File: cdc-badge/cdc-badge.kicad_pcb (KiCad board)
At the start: 4 copper layers, 85 x 110 mm, 158 parts, among them J1 USB_C, J2 JST S2B-PH-SM4-TB, J3 Conn_02x20_Odd_Even, J4 Conn_Grove, J5 Conn_02x03_Odd_Even, J6 Conn_01x06, J7 Conn_01x24, Q1 Si1308EDL, Q2 Si1308EDL, SW0 0, SW1 1, SW10 YES, SW11 NO, SW12 power on/reset, SW13 reset, SW14 flash/power off, SW15 MST-22D18G2 3J, SW16 MST-22D18G2 3J, SW2 2, SW3 3, SW4 4, SW5 5, SW6 6, SW7 7, SW8 8, SW9 9, U1 ESP32-S3-WROOM-1-N16R8, U2 TCA9535PWR, U3 TR01-C2P-T301, U5 TLV61070ADBVR, U6 BQ25895RTW, U8 TLV62569DBV

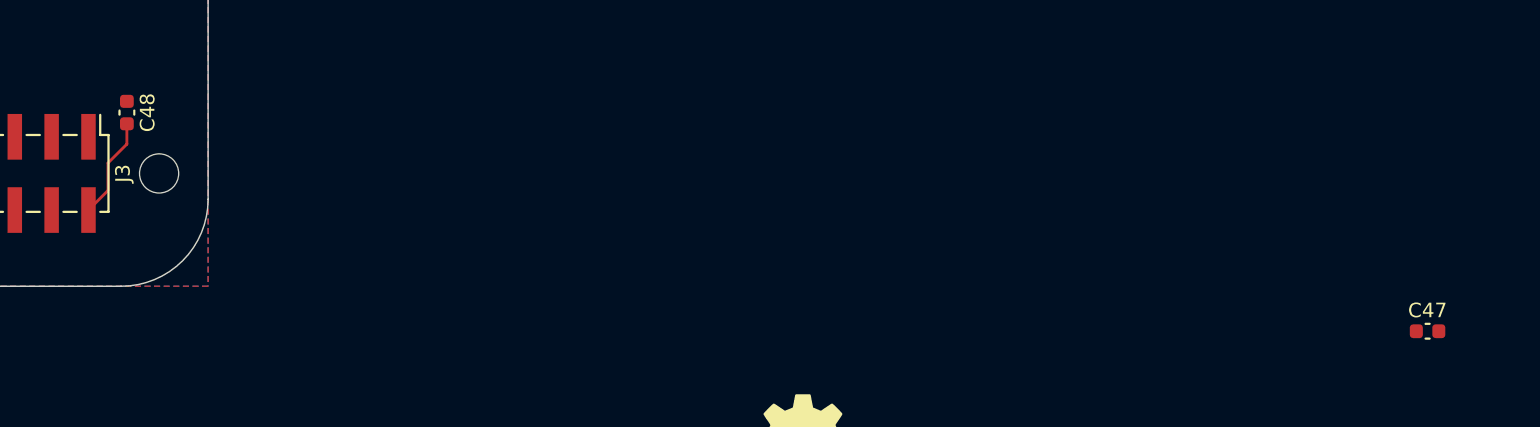
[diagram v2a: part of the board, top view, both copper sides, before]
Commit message: PCB: place caps to 3.3v and 5v pins at raspi conn.
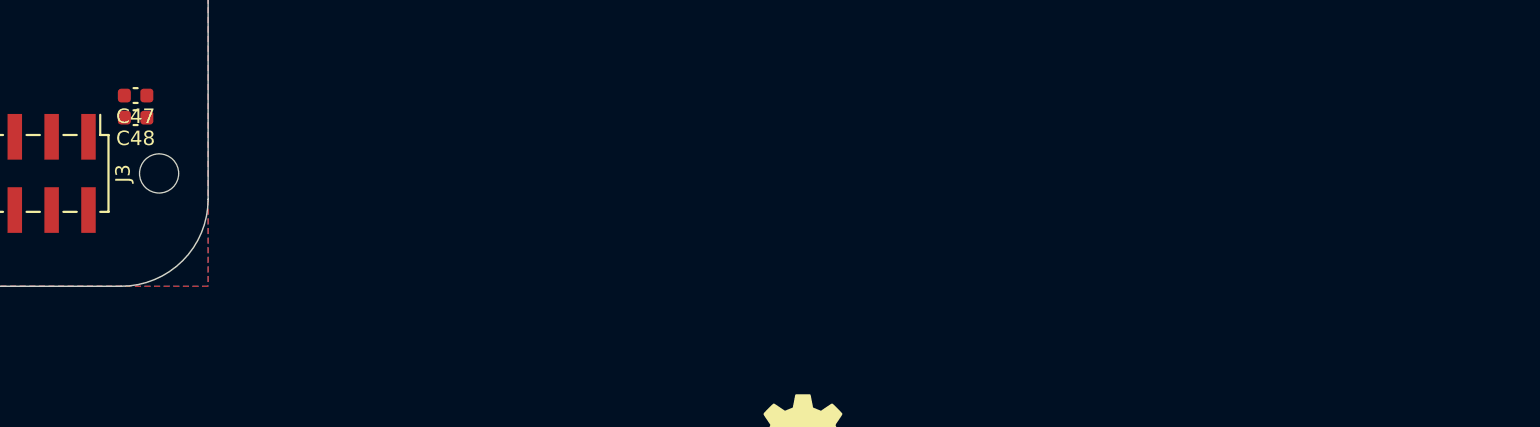
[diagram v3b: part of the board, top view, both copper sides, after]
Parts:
- moved C47 90.5 mm to (135.0, 145.8), turned to 180 degrees
- moved C48 0.69 mm to (135.0, 147.4), turned to 180 degrees
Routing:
- net +5V: track 8.72 -> 1.68 mm
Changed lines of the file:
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@@
 	(footprint "Capacitor_SMD:C_0603_1608Metric"
 		(layer "F.Cu")
-		(at 224.075 162.1)
+		(at 135 145.85 180)
 		(descr "Capacitor SMD 0603 (1608 Metric), square (rectangular) end terminal, IPC-7351 nominal, (Body size source: IPC-SM-782 page 76, https://www.pcb-3d.com/wordpress/wp-content/uploads/ipc-sm-782a_amendment_1_and_2.pdf), generated with kicad-footprint-generator")
 		(tags "capacitor")
@@
 		)
 		(property "MPN" "CL10A105KB8NNNC"
-			(at 0 0 0)
+			(at 0 0 180)
 			(unlocked yes)
 			(layer "F.Fab")
@@
 		)
 		(property "JLCPCB PN" "C15849"
-			(at 0 0 0)
+			(at 0 0 180)
 			(unlocked yes)
 			(layer "F.Fab")
@@
 		(attr smd)
 		(fp_line
-			(start -0.14058 -0.51)
-			(end 0.14058 -0.51)
+			(start -0.14058 0.51)
+			(end 0.14058 0.51)
 			(stroke
 				(width 0.153)
@@
 		)
 		(fp_line
-			(start -0.14058 0.51)
-			(end 0.14058 0.51)
+			(start -0.14058 -0.51)
+			(end 0.14058 -0.51)
 			(stroke
 				(width 0.153)
@@
 		)
 		(fp_line
-			(start -1.48 -0.73)
-			(end 1.48 -0.73)
+			(start 1.48 0.73)
+			(end -1.48 0.73)
 			(stroke
 				(width 0.05)
@@
 		)
 		(fp_line
-			(start -1.48 0.73)
-			(end -1.48 -0.73)
+			(start 1.48 -0.73)
+			(end 1.48 0.73)
 			(stroke
 				(width 0.05)
@@
 		)
 		(fp_line
-			(start 1.48 -0.73)
-			(end 1.48 0.73)
+			(start -1.48 0.73)
+			(end -1.48 -0.73)
 			(stroke
 				(width 0.05)
@@
 		)
 		(fp_line
-			(start 1.48 0.73)
-			(end -1.48 0.73)
+			(start -1.48 -0.73)
+			(end 1.48 -0.73)
 			(stroke
 				(width 0.05)
@@
 		)
 		(fp_line
-			(start -0.8 -0.4)
-			(end 0.8 -0.4)
+			(start 0.8 0.4)
+			(end -0.8 0.4)
 			(stroke
 				(width 0.1)
@@
 		)
 		(fp_line
-			(start -0.8 0.4)
-			(end -0.8 -0.4)
+			(start 0.8 -0.4)
+			(end 0.8 0.4)
 			(stroke
 				(width 0.1)
@@
 		)
 		(fp_line
-			(start 0.8 -0.4)
-			(end 0.8 0.4)
+			(start -0.8 0.4)
+			(end -0.8 -0.4)
 			(stroke
 				(width 0.1)
@@
 		)
 		(fp_line
-			(start 0.8 0.4)
-			(end -0.8 0.4)
+			(start -0.8 -0.4)
+			(end 0.8 -0.4)
 			(stroke
 				(width 0.1)
@@
 		)
 		(pad "1" smd roundrect
-			(at -0.775 0)
+			(at -0.775 0 180)
 			(size 0.9 0.95)
 			(layers "F.Cu" "F.Mask" "F.Paste")
@@
 		)
 		(pad "2" smd roundrect
-			(at 0.775 0)
+			(at 0.775 0 180)
 			(size 0.9 0.95)
 			(layers "F.Cu" "F.Mask" "F.Paste")
@@
 	(footprint "Capacitor_SMD:C_0603_1608Metric"
 		(layer "F.Cu")
-		(at 134.4 147.025 -90)
+		(at 135 147.375 180)
 		(descr "Capacitor SMD 0603 (1608 Metric), square (rectangular) end terminal, IPC-7351 nominal, (Body size source: IPC-SM-782 page 76, https://www.pcb-3d.com/wordpress/wp-content/uploads/ipc-sm-782a_amendment_1_and_2.pdf), generated with kicad-footprint-generator")
 		(tags "capacitor")
 		(property "Reference" "C48"
-			(at 0 -1.43 90)
+			(at 0 -1.43 0)
 			(layer "F.SilkS")
 			(effects
@@
 		)
 		(property "Value" "1uF"
-			(at 0 1.43 90)
+			(at 0 1.43 0)
 			(layer "F.Fab")
 			(effects
@@
 		)
 		(property "Datasheet" "~"
-			(at 0 0 90)
+			(at 0 0 0)
 			(layer "F.Fab")
 			(hide yes)
@@
 		)
 		(property "Description" "1uF 50V X5R ±10% 0603 Multilayer Ceramic Capacitor"
-			(at 0 0 90)
+			(at 0 0 0)
 			(layer "F.Fab")
 			(hide yes)
@@
 		)
 		(property "MPN" "CL10A105KB8NNNC"
-			(at 0 0 270)
+			(at 0 0 180)
 			(unlocked yes)
 			(layer "F.Fab")
@@
 		)
 		(property "JLCPCB PN" "C15849"
-			(at 0 0 270)
+			(at 0 0 180)
 			(unlocked yes)
 			(layer "F.Fab")
@@
 		)
 		(fp_line
-			(start -1.48 0.73)
-			(end -1.48 -0.73)
+			(start 1.48 0.73)
+			(end -1.48 0.73)
 			(stroke
 				(width 0.05)
@@
 		)
 		(fp_line
-			(start 1.48 0.73)
-			(end -1.48 0.73)
+			(start 1.48 -0.73)
+			(end 1.48 0.73)
 			(stroke
 				(width 0.05)
@@
 		)
 		(fp_line
-			(start -1.48 -0.73)
-			(end 1.48 -0.73)
+			(start -1.48 0.73)
+			(end -1.48 -0.73)
 			(stroke
 				(width 0.05)
@@
 		)
 		(fp_line
-			(start 1.48 -0.73)
-			(end 1.48 0.73)
+			(start -1.48 -0.73)
+			(end 1.48 -0.73)
 			(stroke
 				(width 0.05)
@@
 		)
 		(fp_line
-			(start -0.8 0.4)
-			(end -0.8 -0.4)
+			(start 0.8 0.4)
+			(end -0.8 0.4)
 			(stroke
 				(width 0.1)
@@
 		)
 		(fp_line
-			(start 0.8 0.4)
-			(end -0.8 0.4)
+			(start 0.8 -0.4)
+			(end 0.8 0.4)
 			(stroke
 				(width 0.1)
@@
 		)
 		(fp_line
-			(start -0.8 -0.4)
-			(end 0.8 -0.4)
+			(start -0.8 0.4)
+			(end -0.8 -0.4)
 			(stroke
 				(width 0.1)
@@
 		)
 		(fp_line
-			(start 0.8 -0.4)
-			(end 0.8 0.4)
+			(start -0.8 -0.4)
+			(end 0.8 -0.4)
 			(stroke
 				(width 0.1)
@@
 		)
 		(fp_text user "${REFERENCE}"
-			(at 0 0 90)
+			(at 0 0 0)
 			(layer "F.Fab")
 			(effects
@@
 		)
 		(pad "1" smd roundrect
-			(at -0.775 0 270)
+			(at -0.775 0 180)
 			(size 0.9 0.95)
 			(layers "F.Cu" "F.Mask" "F.Paste")
@@
 		)
 		(pad "2" smd roundrect
-			(at 0.775 0 270)
+			(at 0.775 0 180)
 			(size 0.9 0.95)
 			(layers "F.Cu" "F.Mask" "F.Paste")
@@
 	)
 	(segment
-		(start 134.4 149.2)
-		(end 134.4 147.8)
-		(width 0.2)
-		(layer "F.Cu")
-		(net 3)
-	)
-	(segment
-		(start 133.1 150.5)
-		(end 134.4 149.2)
-		(width 0.2)
-		(layer "F.Cu")
-		(net 3)
-	)
-	(segment
 		(start 128.2625 91.6125)
 		(end 128.225 91.575)
@@
 		(layer "F.Cu")
 		(net 3)
-	)
-	(segment
-		(start 133.1 152.3965)
-		(end 133.1 150.5)
-		(width 0.2)
-		(layer "F.Cu")
-		(net 3)
-	)
-	(segment
-		(start 131.7515 153.745)
-		(end 133.1 152.3965)
-		(width 0.2)
-		(layer "F.Cu")
-		(net 3)

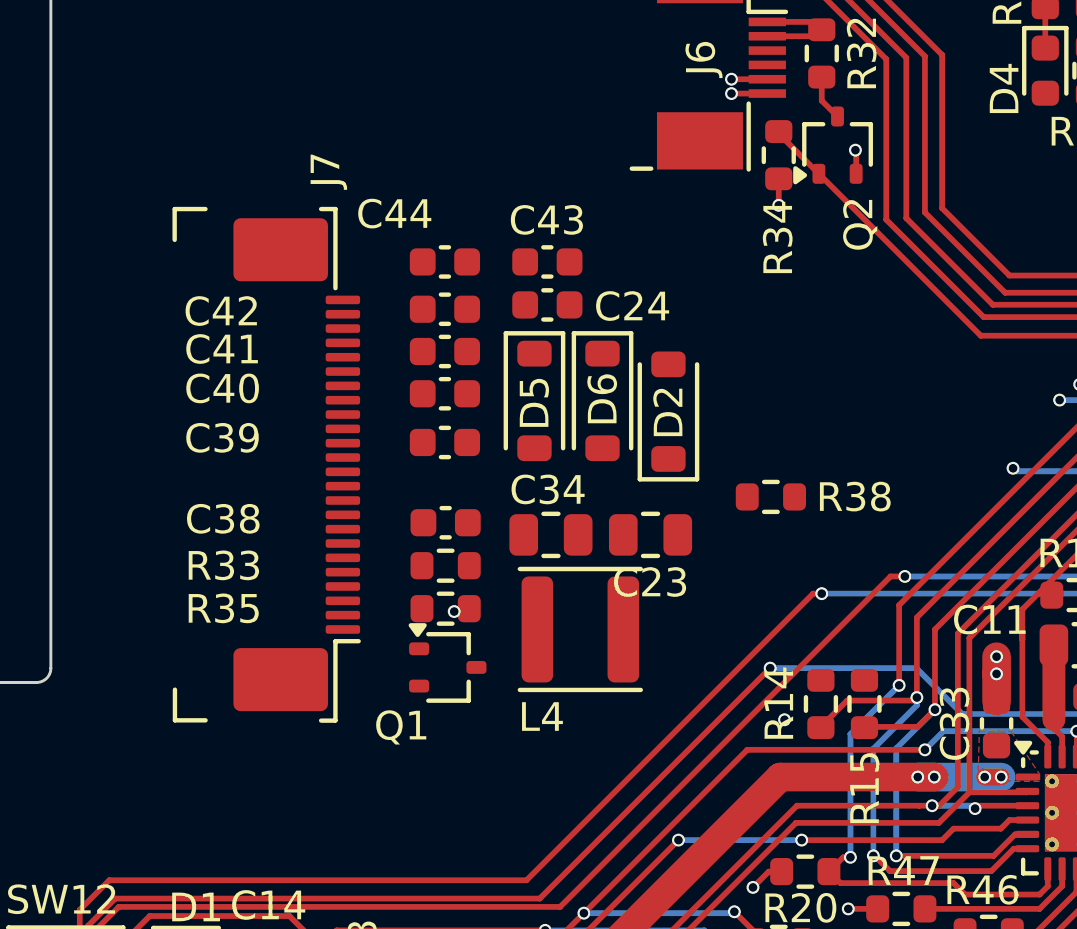
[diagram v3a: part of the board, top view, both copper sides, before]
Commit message: PCB: arrange and connect display components
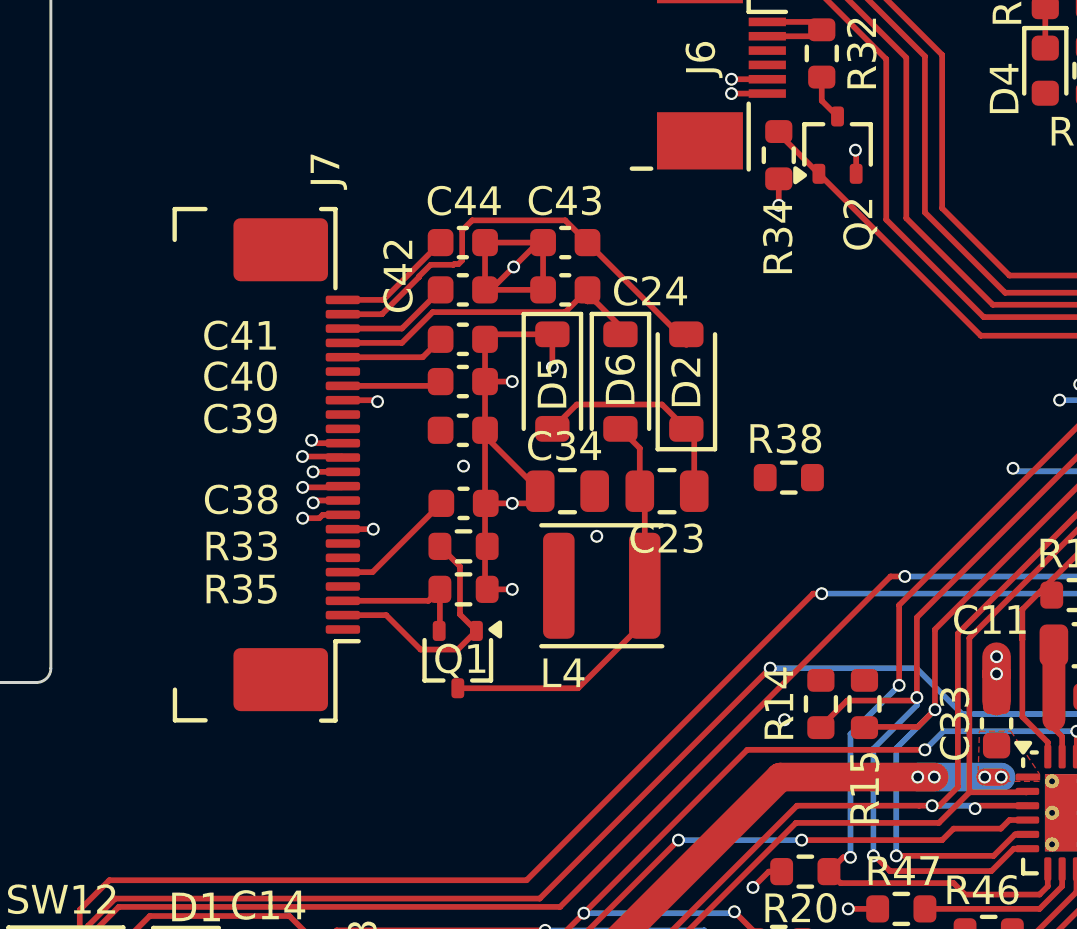
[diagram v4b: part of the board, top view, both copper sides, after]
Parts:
- moved L4 1.70 mm to (77.2, 83.6)
- moved C23 1.63 mm to (79.5, 80.3)
- moved C34 1.63 mm to (76.0, 80.3)
- moved D2 1.22 mm to (80.2, 76.5)
- moved R38 0.92 mm to (83.8, 79.8)
- moved C38 0.92 mm to (72.4, 80.8)
- moved C42 0.92 mm to (72.4, 73.3)
- moved C43 0.92 mm to (76.0, 71.7)
- moved C44 0.92 mm to (72.4, 71.7)
- moved D5 0.92 mm to (75.5, 76.5)
- moved D6 0.92 mm to (77.9, 76.5)
- moved R33 0.92 mm to (72.4, 82.2)
- moved R35 0.92 mm to (72.4, 83.8)
- moved C24 0.82 mm to (76.0, 73.3)
- moved C39 0.76 mm to (72.4, 78.2)
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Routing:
- net GND: track 56.6 -> 88.1 mm, vias 70 -> 76
- net /PREVGL: track 0.00 -> 15.7 mm
- net Net-(D6-A): track 0.00 -> 15.5 mm
- net /PREVGH: track 0.00 -> 12.0 mm
- net /GDR: track 0.00 -> 8.91 mm
- net Net-(D2-K): track 0.00 -> 7.67 mm
- net /RESE: track 0.00 -> 5.01 mm
- net Net-(J7-VSH2): track 0.00 -> 4.43 mm
- net Net-(J7-VCOM): track 0.00 -> 4.24 mm
- net Net-(J7-VSL): track 0.00 -> 3.97 mm
- net Net-(J7-VSH1): track 0.00 -> 3.67 mm
- net Net-(J7-VDD): track 0.00 -> 3.47 mm
- net +3.3V: track 11.4 -> 13.5 mm, vias 9 -> 11
- net /SPI_BUSY_EPD: track 0.00 -> 1.45 mm, vias 0 -> 1
- net /SPI_SCLK: track 24.2 -> 25.6 mm, vias 2 -> 3
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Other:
- board text removed: "Epaper"

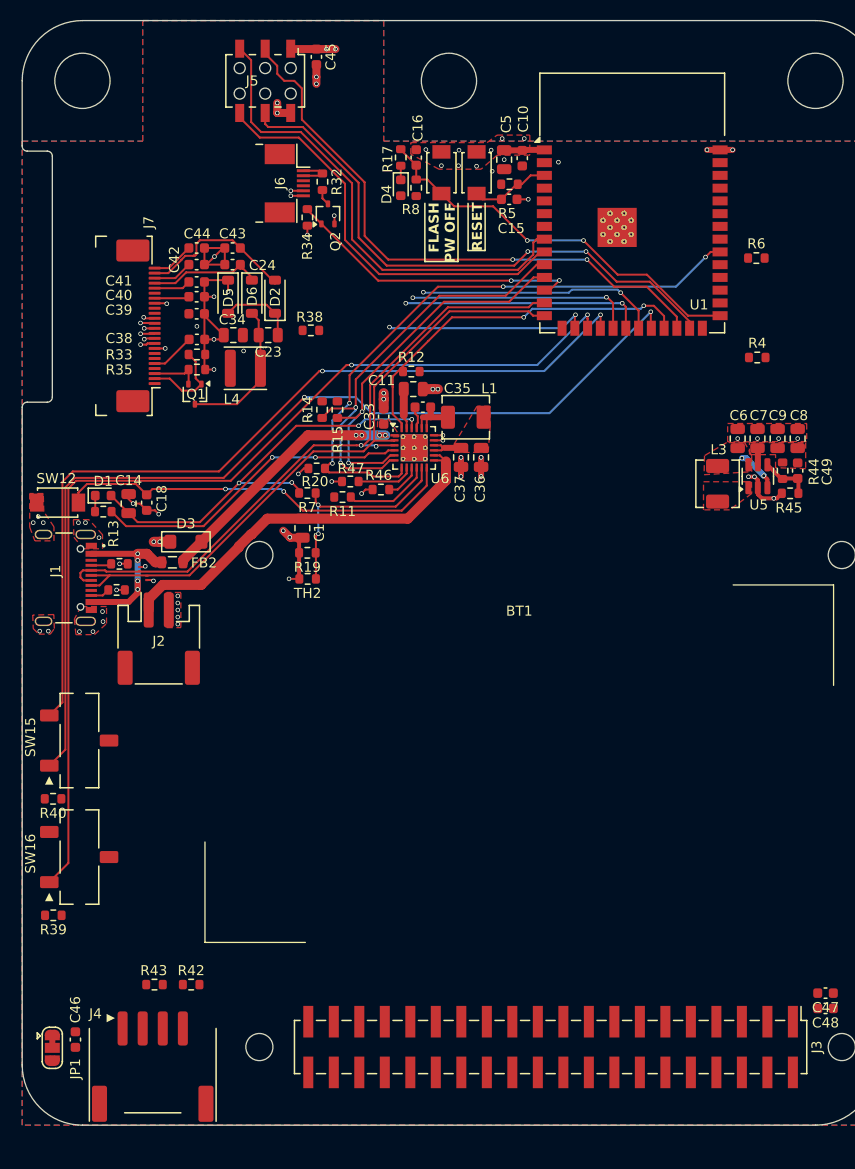
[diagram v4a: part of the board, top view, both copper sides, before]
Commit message: PCB: route SPI connections and others
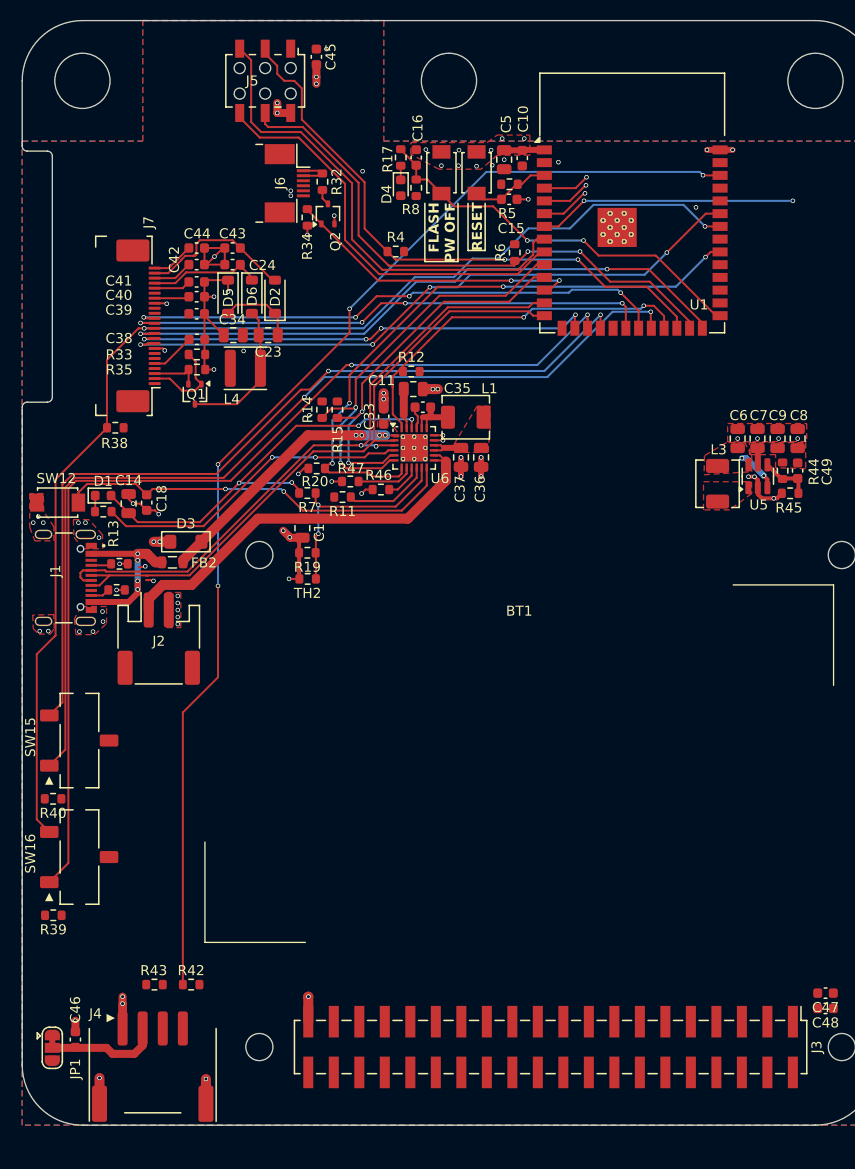
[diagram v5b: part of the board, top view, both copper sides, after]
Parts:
- moved R4 37.5 mm to (92.2, 72.0)
- moved R6 24.1 mm to (104.0, 72.1), turned to 90 degrees
- moved R38 21.8 mm to (64.3, 89.5), turned to 180 degrees
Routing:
- net /SPI_CS_EPD: track 1.04 -> 119.8 mm, vias 1 -> 2
- net /GROVE0: track 0.00 -> 116.9 mm, vias 0 -> 4
- net /SPI_BUSY_EPD: track 1.45 -> 64.6 mm, vias 1 -> 4
- net /SPI_DC_EPD: track 1.42 -> 62.8 mm, vias 1 -> 2
- net /SPI_MOSI: track 25.3 -> 54.2 mm, vias 3 -> 4
- net /SPI_SCLK: track 25.6 -> 52.9 mm, vias 3 -> 4
- net /PCM_DOUT: track 0.00 -> 25.8 mm, vias 0 -> 2
- net /SPI_RST_EPD: track 21.6 -> 46.4 mm, vias 3 -> 4
- net /SPI_MISO: track 22.7 -> 0.00 mm, vias 2 -> 0
- net GND: track 88.1 -> 100.5 mm, vias 76 -> 81
- net Net-(J4-VCC): track 0.00 -> 11.4 mm
- net +3.3V: track 13.5 -> 6.57 mm
- net /PCM_DIN: track 0.00 -> 4.89 mm, vias 0 -> 1
- net /PCM_FS: track 0.00 -> 4.80 mm, vias 0 -> 1
- net /PCM_CLK: track 0.00 -> 4.65 mm, vias 0 -> 1
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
